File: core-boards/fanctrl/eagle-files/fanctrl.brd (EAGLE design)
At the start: 50.8 x 50.8 mm, 32 parts, among them J1 3-PIN_2MM-H, U1 MCP9701T-E/TT

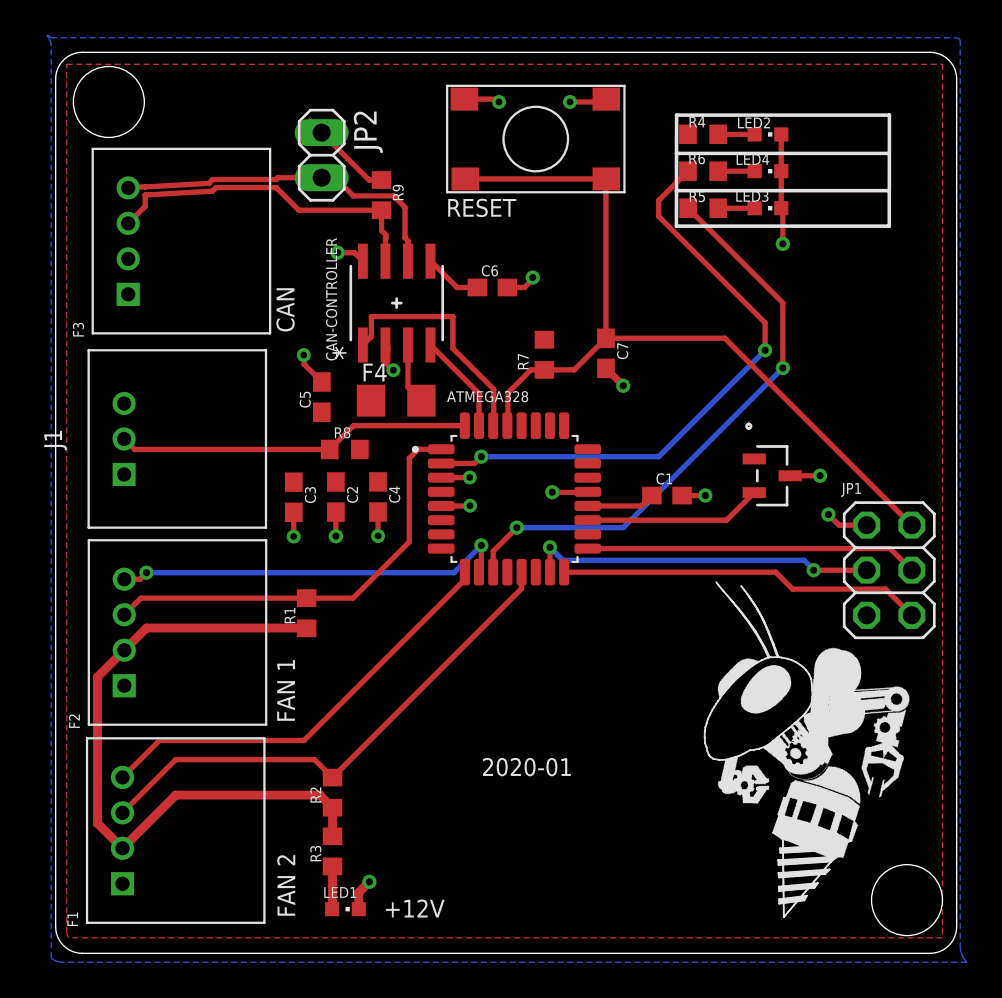
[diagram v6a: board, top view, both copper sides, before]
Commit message: Fix LED routing. Fix LED name (ERROR --> INVALID TEMP).
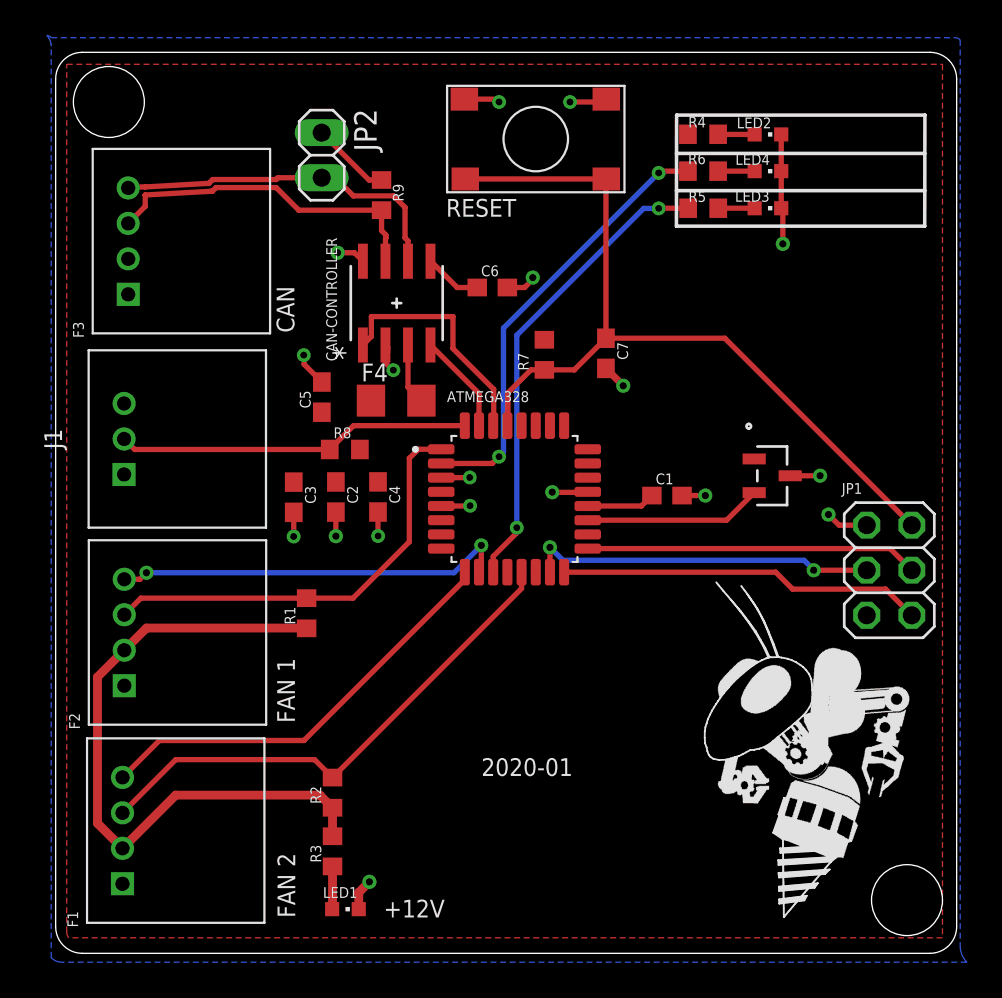
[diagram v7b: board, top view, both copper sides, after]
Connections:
- net ERROR-LED renamed INVALID-TEMP-LED
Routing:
- net STATUS-READY-LED: track 34.2 -> 24.8 mm
- net INVALID-TEMP-LED: track 33.0 -> 26.5 mm
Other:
- board text added: "BAD TEMP"
- board text removed: "ERROR"
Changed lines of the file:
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@@
 <vertex x="39" y="2"/>
 </polygon>
-<text x="42" y="41.52" size="1" layer="51" font="vector" ratio="16">ERROR</text>
+<text x="42" y="41.52" size="1" layer="51" font="vector" ratio="16">BAD TEMP</text>
 <text x="41.99" y="43.58" size="1" layer="51" font="vector" ratio="16">READY</text>
 <text x="42" y="45.73" size="1" layer="51" font="vector" ratio="16">+5V</text>
@@
 <text x="13.51" y="2" size="1" layer="21" font="vector" rot="R90">FAN 2</text>
 <text x="22.01" y="41.53" size="1" layer="21" font="vector">RESET</text>
-<wire x1="35" y1="41" x2="47" y2="41" width="0.2" layer="21"/>
-<wire x1="47" y1="41" x2="47.01" y2="47.26" width="0.2" layer="21"/>
-<wire x1="47.01" y1="47.26" x2="35.01" y2="47.26" width="0.2" layer="21"/>
+<wire x1="35" y1="41" x2="49" y2="41" width="0.2" layer="21"/>
+<wire x1="49" y1="41" x2="49.01" y2="47.26" width="0.2" layer="21"/>
+<wire x1="49.01" y1="47.26" x2="35.01" y2="47.26" width="0.2" layer="21"/>
 <wire x1="35.01" y1="47.26" x2="35" y2="41" width="0.2" layer="21"/>
-<wire x1="35" y1="45.1" x2="47" y2="45.1" width="0.2" layer="21"/>
-<wire x1="35" y1="43" x2="47" y2="43" width="0.2" layer="21"/>
+<wire x1="35" y1="45.1" x2="49" y2="45.1" width="0.2" layer="21"/>
+<wire x1="35" y1="43" x2="49" y2="43" width="0.2" layer="21"/>
 <text x="24" y="10" size="1" layer="21" font="vector">2020-01</text>
 <text x="18.49" y="2.02" size="1" layer="21" font="vector" ratio="16">+12V</text>
@@
 <wire x1="37.36" y1="46.17" x2="37.35" y2="46.18" width="0.3" layer="1"/>
 </signal>
-<signal name="ERROR-LED">
+<signal name="INVALID-TEMP-LED">
 <contactref element="ATMEGA328" pad="11"/>
 <contactref element="R5" pad="2"/>
-<via x="41" y="33" extent="1-16" drill="0.4" diameter="0.65"/>
-<wire x1="41" y1="33" x2="32" y2="24" width="0.3" layer="16"/>
-<wire x1="32" y1="24" x2="26" y2="24" width="0.3" layer="16"/>
-<via x="26" y="24" extent="1-16" drill="0.4" diameter="0.65"/>
-<wire x1="26" y1="24" x2="24.67" y2="22.67" width="0.3" layer="1"/>
-<wire x1="24.67" y1="22.67" x2="24.67" y2="21.49" width="0.3" layer="1"/>
-<wire x1="41" y1="33" x2="41" y2="36.67" width="0.3" layer="1"/>
-<wire x1="41" y1="36.67" x2="35.66" y2="42.01" width="0.3" layer="1"/>
+<wire x1="24.67" y1="21.49" x2="24.67" y2="22.38" width="0.3" layer="1"/>
+<wire x1="26" y1="23.71" x2="26" y2="24" width="0.3" layer="1"/>
+<via x="26" y="24" extent="1-16" drill="0.381"/>
+<wire x1="26" y1="24" x2="26" y2="34.85" width="0.3" layer="16"/>
+<wire x1="33.15" y1="42" x2="26" y2="34.85" width="0.3" layer="16"/>
+<wire x1="33.15" y1="42" x2="34" y2="42" width="0.3" layer="16"/>
+<via x="34" y="42" extent="1-16" drill="0.381"/>
+<wire x1="34" y1="42" x2="34.01" y2="42.01" width="0.3" layer="1"/>
+<wire x1="34.01" y1="42.01" x2="35.66" y2="42.01" width="0.3" layer="1"/>
+<wire x1="24.67" y1="22.38" x2="26" y2="23.71" width="0.3" layer="1"/>
 </signal>
 <signal name="N$4">
@@
 <contactref element="R6" pad="2"/>
 <contactref element="ATMEGA328" pad="2"/>
-<via x="40" y="34" extent="1-16" drill="0.4" diameter="0.65"/>
-<wire x1="40" y1="34" x2="34" y2="28" width="0.3" layer="16"/>
-<wire x1="34" y1="28" x2="24" y2="28" width="0.3" layer="16"/>
-<via x="24" y="28" extent="1-16" drill="0.4" diameter="0.65"/>
-<wire x1="24" y1="28" x2="23.62" y2="27.62" width="0.3" layer="1"/>
-<wire x1="23.62" y1="27.62" x2="21.74" y2="27.62" width="0.3" layer="1"/>
-<wire x1="40" y1="34" x2="40" y2="35.55" width="0.3" layer="1"/>
-<wire x1="40" y1="35.55" x2="34" y2="41.55" width="0.3" layer="1"/>
-<wire x1="34" y1="41.55" x2="34" y2="42.45" width="0.3" layer="1"/>
-<wire x1="34" y1="42.45" x2="35.65" y2="44.1" width="0.3" layer="1"/>
+<via x="25" y="28" extent="1-16" drill="0.381"/>
+<wire x1="25" y1="28" x2="25.25" y2="28.25" width="0.3" layer="16"/>
+<wire x1="25.25" y1="35.25" x2="25.25" y2="28.25" width="0.3" layer="16"/>
+<via x="34" y="44" extent="1-16" drill="0.381"/>
+<wire x1="34" y1="44" x2="34.1" y2="44.1" width="0.3" layer="1"/>
+<wire x1="34.1" y1="44.1" x2="35.65" y2="44.1" width="0.3" layer="1"/>
+<wire x1="25.25" y1="35.25" x2="34" y2="44" width="0.3" layer="16"/>
+<wire x1="25" y1="28" x2="24.62" y2="27.62" width="0.3" layer="1"/>
+<wire x1="24.62" y1="27.62" x2="21.74" y2="27.62" width="0.3" layer="1"/>
 </signal>
 <signal name="!RESET">

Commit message: Fix decoupling CAP locations.
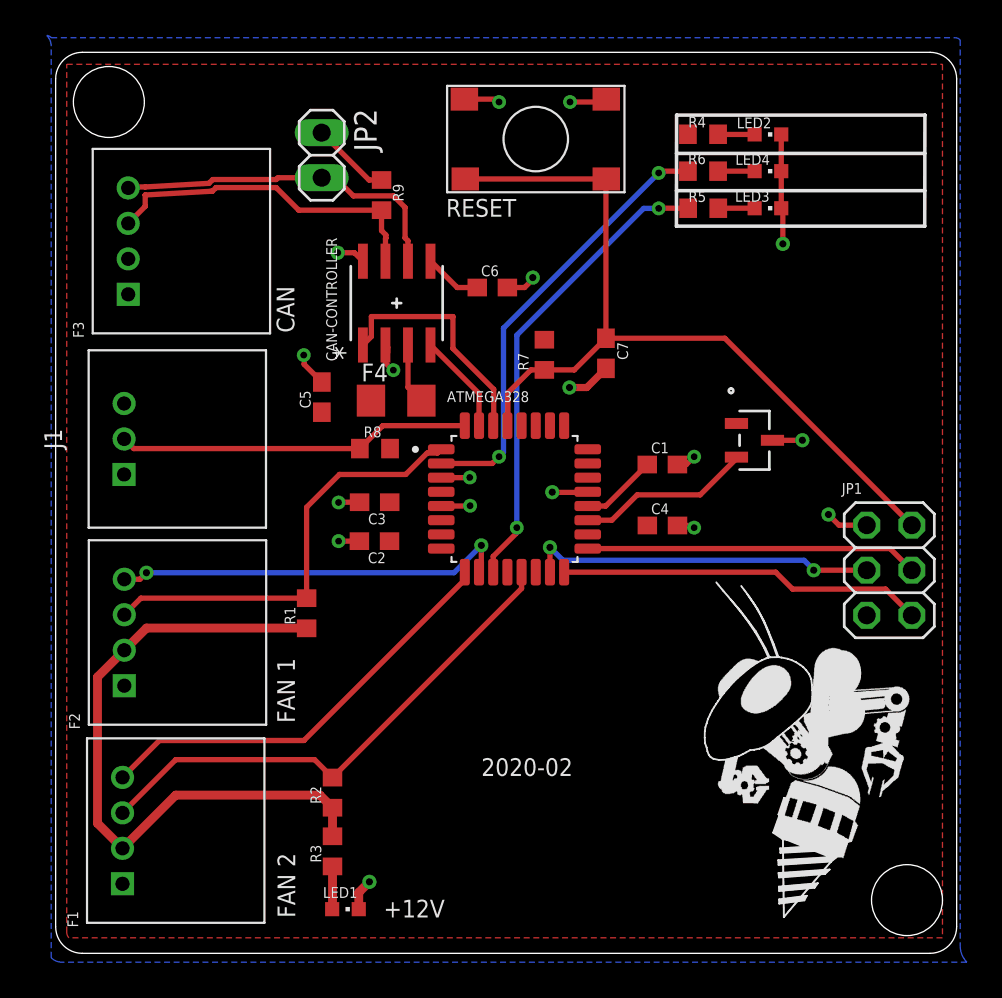
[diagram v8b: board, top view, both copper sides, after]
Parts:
- moved C4 16.1 mm to (34.2, 24.1), turned to 0 degrees
- moved C3 4.57 mm to (18.0, 25.4), turned to 180 degrees
- moved C2 3.30 mm to (18.0, 23.2), turned to 180 degrees
- moved U1 2.24 mm to (39.4, 28.9)
- moved C1 1.77 mm to (34.2, 27.6)
- moved R8 1.70 mm to (18.0, 28.5)
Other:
- board text added: "2020-02"
- board text removed: "2020-01"
